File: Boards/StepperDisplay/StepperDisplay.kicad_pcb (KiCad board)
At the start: 2 copper layers, 120.4 x 102.1 mm, 113 parts, among them IC1 ATTINY861-P, P1 CONN_01X06, P2 ISP, Q1 BC857, Q10 BC857, Q11 BC857, Q12 BC857, Q13 BC857, Q14 BC857, Q15 BC857, Q16 BC857, Q17 BC857, Q18 BC857, Q2 BC857, Q3 BC857, Q4 BC857, Q5 BC857, Q6 BC857, Q7 BC857, Q8 BC857, Q9 BC857, SW1 SW_PUSH, SW2 SW_PUSH, U1 74HC595, U2 74HC595, U3 ULN2801A, U4 74HC595, U5 74HC595, U6 ULN2801A, U7 74HC595, U8 74HC595, U9 ULN2801A, X1 CRYSTAL_SMD

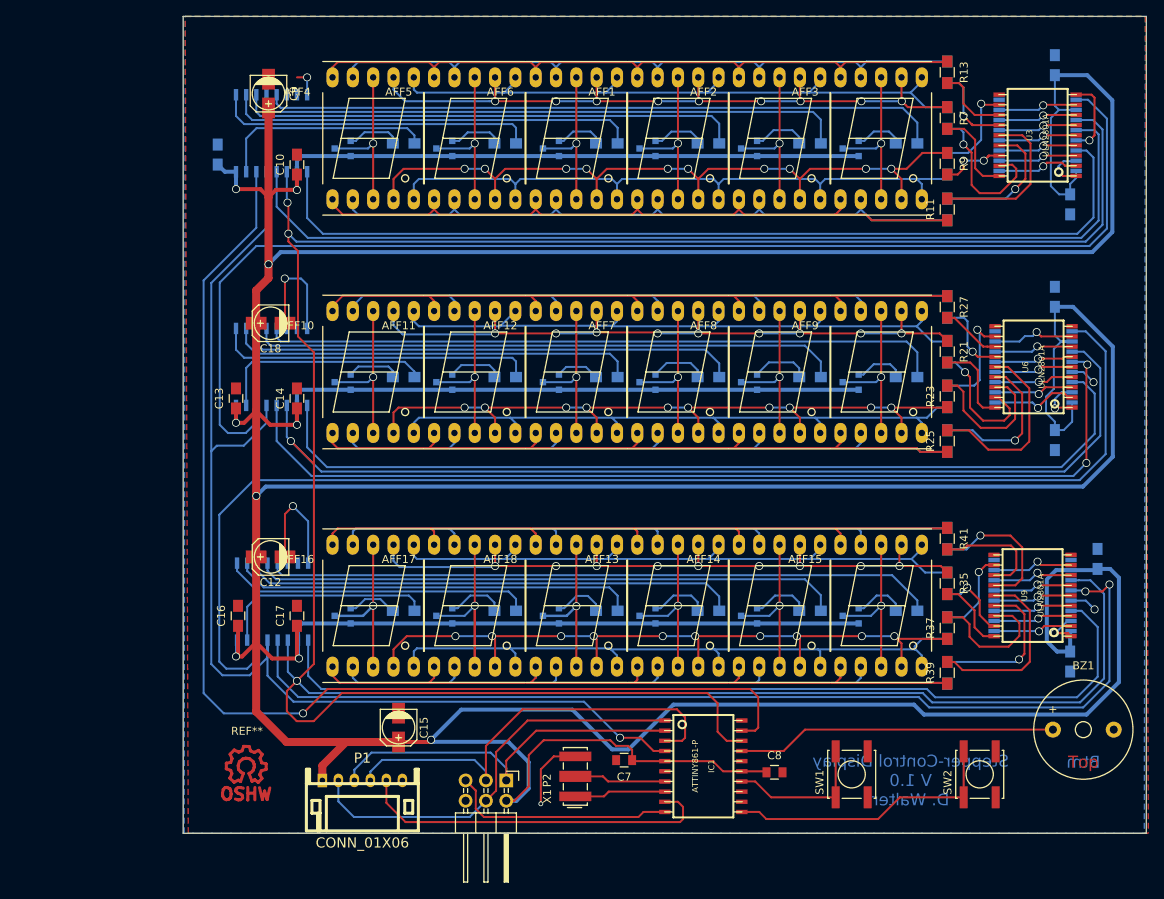
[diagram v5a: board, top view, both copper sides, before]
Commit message: Changed to segment multiplexing, new layout
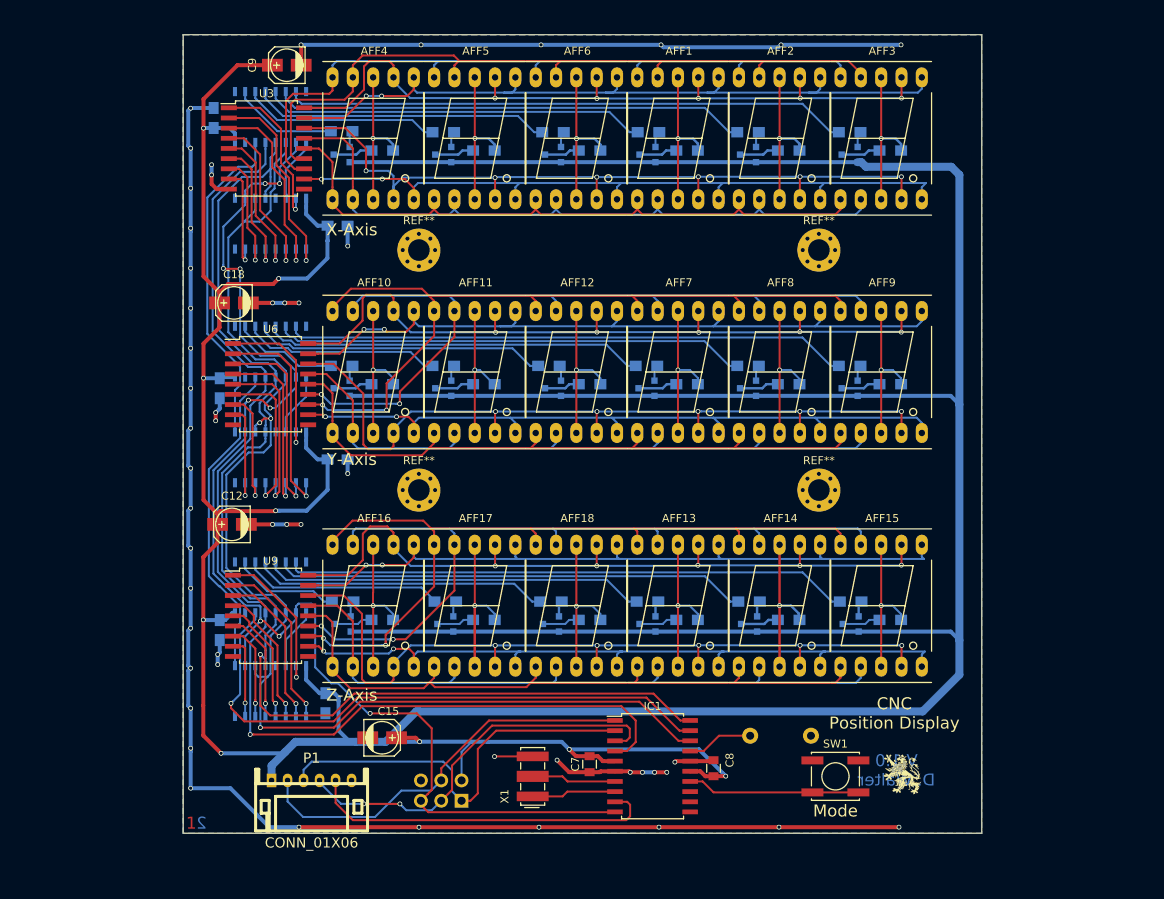
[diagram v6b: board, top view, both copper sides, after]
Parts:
- removed C1, C2, C3, C4, C5, C6: 100nF, Capacitors_SMD:C_0805_HandSoldering
- removed R13, R14, R27, R28, R41, R42: R, Resistors_SMD:R_0805_HandSoldering
- removed the REF** at (74.9, 133.1)
- removed SW2: SW_PUSH, Buttons_Switches_SMD:SW_SPST_EVPBF
- added G***: LOGO, Loewe:Loewe_Klein, F.Cu at (157.0, 134.1)
- added REF**: MountingHole_2.7mm_M2.5_Pad_Via, Mounting_Holes:MountingHole_2.7mm_M2.5_Pad_Via, F.Cu at (96.5, 98.6)
- added REF**: MountingHole_2.7mm_M2.5_Pad_Via, Mounting_Holes:MountingHole_2.7mm_M2.5_Pad_Via, F.Cu at (146.5, 98.6)
- added REF**: MountingHole_2.7mm_M2.5_Pad_Via, Mounting_Holes:MountingHole_2.7mm_M2.5_Pad_Via, F.Cu at (96.5, 68.6)
- added REF**: MountingHole_2.7mm_M2.5_Pad_Via, Mounting_Holes:MountingHole_2.7mm_M2.5_Pad_Via, F.Cu at (146.5, 68.6)
- BZ1, C10, C13, C14, C16, C17, R11, R21, R23, R25, R35, R37, R39, R7, R9: moved to B.Cu
- IC1: footprint w_smd_dil:soic-20 -> Housings_SOIC:SOIC-20_7.5x12.8mm_Pitch1.27mm
- P2: footprint Pin_Headers:Pin_Header_Angled_2x03 -> Pin_Headers:Pin_Header_Straight_2x03; moved to B.Cu
- Q1, Q10, Q11, Q12, Q13, Q14, Q15, Q16, Q17, Q18, Q2, Q3, Q4, Q5, Q6, Q7, Q8, Q9: footprint Housings_SOT-23_SOT-143_TSOT-6:SOT-23 -> TO_SOT_Packages_SMD:SOT-23
- U1, U2, U4, U5, U7, U8: footprint w_smd_dil:soic-16 -> SMD_Packages:SO-16-N
- U3, U6, U9: footprint w_smd_dil:soic-18 -> Housings_SOIC:SOIC-18_7.5x11.6mm_Pitch1.27mm
- moved U2 96.5 mm to (78.0, 65.3), turned to 180 degrees
- moved U3 96.4 mm to (77.5, 55.9), turned to 0 degrees
- moved U5 96.0 mm to (78.0, 94.5), turned to 180 degrees
- moved U8 96.0 mm to (78.0, 123.7), turned to 180 degrees
- moved U6 95.4 mm to (78.0, 85.3), turned to 0 degrees
- moved U9 95.3 mm to (78.0, 114.3), turned to 0 degrees
- moved R35 70.8 mm to (91.9, 114.8), turned to 0 degrees
- moved R21 70.7 mm to (91.9, 85.3), turned to 0 degrees
- moved R7 70.7 mm to (91.9, 56.1), turned to 0 degrees
- moved R36 58.1 mm to (104.6, 114.8), turned to 0 degrees
- moved R22 58.1 mm to (104.6, 85.3), turned to 0 degrees
- moved R8 58.1 mm to (104.6, 56.1), turned to 0 degrees
- moved R9 44.7 mm to (117.9, 56.1), turned to 0 degrees
- moved R23 44.7 mm to (117.9, 85.3), turned to 0 degrees
- moved R37 44.7 mm to (117.9, 114.8), turned to 0 degrees
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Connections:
- net CS renamed Net-(IC1-Pad9)
- net MISO renamed Net-(IC1-Pad2)
- net MOSI renamed Net-(IC1-Pad1)
- net SCK renamed Net-(IC1-Pad3)
- IC1 pad 10: Net-(IC1-Pad10) -> /Controller/Reset
- IC1 pad 11: Net-(IC1-Pad11) -> (no net)
- IC1 pad 19: /LEDsX/Ser_In -> /LEDsZ/Ser_In
- IC1 pad 20: (no net) -> /Controller/R_Clock
- P2 pad 5: Net-(IC1-Pad10) -> /Controller/Reset
- Q1 pad 3: Net-(AFF4-Pad3) -> Net-(Q1-Pad3)
- Q10 pad 3: Net-(AFF7-Pad3) -> Net-(Q10-Pad3)
- Q11 pad 3: Net-(AFF8-Pad3) -> Net-(Q11-Pad3)
- Q12 pad 3: Net-(AFF9-Pad3) -> Net-(Q12-Pad3)
- Q13 pad 3: Net-(AFF16-Pad3) -> Net-(Q13-Pad3)
- Q14 pad 3: Net-(AFF17-Pad3) -> Net-(Q14-Pad3)
- Q15 pad 3: Net-(AFF18-Pad3) -> Net-(Q15-Pad3)
- Q16 pad 3: Net-(AFF13-Pad3) -> Net-(Q16-Pad3)
- Q17 pad 3: Net-(AFF14-Pad3) -> Net-(Q17-Pad3)
- Q18 pad 3: Net-(AFF15-Pad3) -> Net-(Q18-Pad3)
- Q2 pad 3: Net-(AFF5-Pad3) -> Net-(Q2-Pad3)
- Q3 pad 3: Net-(AFF6-Pad3) -> Net-(Q3-Pad3)
- Q4 pad 3: Net-(AFF1-Pad3) -> Net-(Q4-Pad3)
- Q5 pad 3: Net-(AFF2-Pad3) -> Net-(Q5-Pad3)
- Q6 pad 3: Net-(AFF3-Pad3) -> Net-(Q6-Pad3)
- Q7 pad 3: Net-(AFF10-Pad3) -> Net-(Q7-Pad3)
- Q8 pad 3: Net-(AFF11-Pad3) -> Net-(Q8-Pad3)
- Q9 pad 3: Net-(AFF12-Pad3) -> Net-(Q9-Pad3)
- R10 pad 1: Net-(AFF1-Pad2) -> Net-(Q4-Pad3)
- R10 pad 2: Net-(R10-Pad2) -> Net-(AFF1-Pad3)
- R11 pad 1: Net-(AFF1-Pad1) -> Net-(Q5-Pad3)
- R11 pad 2: Net-(R11-Pad2) -> Net-(AFF2-Pad3)
- R12 pad 1: Net-(AFF1-Pad9) -> Net-(Q6-Pad3)
- R12 pad 2: Net-(R12-Pad2) -> Net-(AFF3-Pad3)
- R21 pad 1: Net-(AFF10-Pad7) -> Net-(Q7-Pad3)
- R21 pad 2: Net-(R21-Pad2) -> Net-(AFF10-Pad3)
- R22 pad 1: Net-(AFF10-Pad6) -> Net-(Q8-Pad3)
- R22 pad 2: Net-(R22-Pad2) -> Net-(AFF11-Pad3)
- R23 pad 1: Net-(AFF10-Pad4) -> Net-(Q9-Pad3)
- R23 pad 2: Net-(R23-Pad2) -> Net-(AFF12-Pad3)
- R24 pad 1: Net-(AFF10-Pad2) -> Net-(Q10-Pad3)
- R24 pad 2: Net-(R24-Pad2) -> Net-(AFF7-Pad3)
- R25 pad 1: Net-(AFF10-Pad1) -> Net-(Q11-Pad3)
- R25 pad 2: Net-(R25-Pad2) -> Net-(AFF8-Pad3)
- R26 pad 1: Net-(AFF10-Pad9) -> Net-(Q12-Pad3)
- R26 pad 2: Net-(R26-Pad2) -> Net-(AFF9-Pad3)
- R35 pad 1: Net-(AFF13-Pad7) -> Net-(Q13-Pad3)
- R35 pad 2: Net-(R35-Pad2) -> Net-(AFF16-Pad3)
- R36 pad 1: Net-(AFF13-Pad6) -> Net-(Q14-Pad3)
- R36 pad 2: Net-(R36-Pad2) -> Net-(AFF17-Pad3)
- R37 pad 1: Net-(AFF13-Pad4) -> Net-(Q15-Pad3)
- R37 pad 2: Net-(R37-Pad2) -> Net-(AFF18-Pad3)
- R38 pad 1: Net-(AFF13-Pad2) -> Net-(Q16-Pad3)
- R38 pad 2: Net-(R38-Pad2) -> Net-(AFF13-Pad3)
- R39 pad 1: Net-(AFF13-Pad1) -> Net-(Q17-Pad3)
- R39 pad 2: Net-(R39-Pad2) -> Net-(AFF14-Pad3)
- R40 pad 1: Net-(AFF13-Pad9) -> Net-(Q18-Pad3)
- R40 pad 2: Net-(R40-Pad2) -> Net-(AFF15-Pad3)
- R7 pad 1: Net-(AFF1-Pad7) -> Net-(Q1-Pad3)
- R7 pad 2: Net-(R7-Pad2) -> Net-(AFF4-Pad3)
- R8 pad 1: Net-(AFF1-Pad6) -> Net-(Q2-Pad3)
- R8 pad 2: Net-(R8-Pad2) -> Net-(AFF5-Pad3)
- R9 pad 1: Net-(AFF1-Pad4) -> Net-(Q3-Pad3)
- R9 pad 2: Net-(R9-Pad2) -> Net-(AFF6-Pad3)
- U1 pad 1: Net-(R2-Pad2) -> (no net)
- U1 pad 10: +5V -> /Controller/Reset
- U1 pad 12: /LEDsX/R_Clock -> /Controller/R_Clock
- U1 pad 15: Net-(R1-Pad2) -> (no net)
- U1 pad 2: Net-(R3-Pad2) -> Net-(R1-Pad2)
- U1 pad 3: Net-(R4-Pad2) -> Net-(R2-Pad2)
- U1 pad 4: Net-(R5-Pad2) -> Net-(R3-Pad2)
- U1 pad 5: Net-(R6-Pad2) -> Net-(R4-Pad2)
- U1 pad 6: (no net) -> Net-(R5-Pad2)
- U1 pad 7: (no net) -> Net-(R6-Pad2)
- U2 pad 10: +5V -> /Controller/Reset
- U2 pad 12: /LEDsX/R_Clock -> /Controller/R_Clock
- U2 pad 9: /LEDsY/Ser_In -> (no net)
- U3 pad 11: Net-(R14-Pad2) -> Net-(AFF1-Pad5)
- U3 pad 12: Net-(R13-Pad2) -> Net-(AFF1-Pad10)
- U3 pad 13: Net-(R12-Pad2) -> Net-(AFF1-Pad9)
- U3 pad 14: Net-(R11-Pad2) -> Net-(AFF1-Pad1)
- U3 pad 15: Net-(R10-Pad2) -> Net-(AFF1-Pad2)
- U3 pad 16: Net-(R9-Pad2) -> Net-(AFF1-Pad4)
- U3 pad 17: Net-(R8-Pad2) -> Net-(AFF1-Pad6)
- U3 pad 18: Net-(R7-Pad2) -> Net-(AFF1-Pad7)
- U4 pad 1: Net-(R16-Pad2) -> (no net)
- U4 pad 10: +5V -> /Controller/Reset
- U4 pad 12: /LEDsY/R_Clock -> /Controller/R_Clock
- U4 pad 15: Net-(R15-Pad2) -> (no net)
- U4 pad 2: Net-(R17-Pad2) -> Net-(R15-Pad2)
- U4 pad 3: Net-(R18-Pad2) -> Net-(R16-Pad2)
- U4 pad 4: Net-(R19-Pad2) -> Net-(R17-Pad2)
- U4 pad 5: Net-(R20-Pad2) -> Net-(R18-Pad2)
- U4 pad 6: (no net) -> Net-(R19-Pad2)
- U4 pad 7: (no net) -> Net-(R20-Pad2)
- U5 pad 10: +5V -> /Controller/Reset
- U5 pad 12: /LEDsY/R_Clock -> /Controller/R_Clock
- U5 pad 9: /LEDsZ/Ser_In -> /LEDsX/Ser_In
- U6 pad 11: Net-(R28-Pad2) -> Net-(AFF10-Pad5)
- U6 pad 12: Net-(R27-Pad2) -> Net-(AFF10-Pad10)
- U6 pad 13: Net-(R26-Pad2) -> Net-(AFF10-Pad9)
- U6 pad 14: Net-(R25-Pad2) -> Net-(AFF10-Pad1)
- U6 pad 15: Net-(R24-Pad2) -> Net-(AFF10-Pad2)
- U6 pad 16: Net-(R23-Pad2) -> Net-(AFF10-Pad4)
- U6 pad 17: Net-(R22-Pad2) -> Net-(AFF10-Pad6)
- U6 pad 18: Net-(R21-Pad2) -> Net-(AFF10-Pad7)
- U7 pad 1: Net-(R30-Pad2) -> (no net)
- U7 pad 10: +5V -> /Controller/Reset
- U7 pad 12: /LEDsZ/R_Clock -> /Controller/R_Clock
- U7 pad 15: Net-(R29-Pad2) -> (no net)
- U7 pad 2: Net-(R31-Pad2) -> Net-(R29-Pad2)
- U7 pad 3: Net-(R32-Pad2) -> Net-(R30-Pad2)
- U7 pad 4: Net-(R33-Pad2) -> Net-(R31-Pad2)
- U7 pad 5: Net-(R34-Pad2) -> Net-(R32-Pad2)
- U7 pad 6: (no net) -> Net-(R33-Pad2)
- U7 pad 7: (no net) -> Net-(R34-Pad2)
- U8 pad 10: +5V -> /Controller/Reset
- U8 pad 12: /LEDsZ/R_Clock -> /Controller/R_Clock
- U8 pad 9: (no net) -> /LEDsY/Ser_In
- U9 pad 11: Net-(R42-Pad2) -> Net-(AFF13-Pad5)
- U9 pad 12: Net-(R41-Pad2) -> Net-(AFF13-Pad10)
- U9 pad 13: Net-(R40-Pad2) -> Net-(AFF13-Pad9)
- U9 pad 14: Net-(R39-Pad2) -> Net-(AFF13-Pad1)
- U9 pad 15: Net-(R38-Pad2) -> Net-(AFF13-Pad2)
- U9 pad 16: Net-(R37-Pad2) -> Net-(AFF13-Pad4)
- U9 pad 17: Net-(R36-Pad2) -> Net-(AFF13-Pad6)
- U9 pad 18: Net-(R35-Pad2) -> Net-(AFF13-Pad7)
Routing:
- net /Controller/Ser_Clock: track 502.8 -> 159.6 mm, vias 4 -> 3
- net +5V: track 888.5 -> 629.5 mm
- net GND: track 57.9 -> 309.1 mm, vias 7 -> 51
- net /Controller/Reset: track 0.00 -> 159.8 mm, vias 0 -> 9
- net /Controller/R_Clock: track 0.00 -> 150.8 mm, vias 0 -> 1
- net /LEDsZ/R_Clock: track 128.8 -> 0.00 mm, vias 2 -> 0
- net /LEDsX/R_Clock: track 123.4 -> 0.00 mm
- net /LEDsY/R_Clock: track 122.6 -> 0.00 mm, vias 2 -> 0
- net /LEDsY/Ser_In: track 157.7 -> 40.4 mm
- net Net-(U7-Pad9): track 115.7 -> 7.66 mm
- net Net-(U1-Pad9): track 115.8 -> 8.04 mm
- net Net-(U4-Pad9): track 115.3 -> 7.91 mm
- net /LEDsX/Ser_In: track 146.0 -> 41.7 mm, vias 1 -> 0
- net /LEDsZ/Ser_In: track 158.3 -> 74.2 mm, vias 0 -> 1
- net Net-(IC1-Pad11): track 35.0 -> 0.00 mm
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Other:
- board size 120.4 x 102.1 mm -> 99.8 x 99.8 mm
- board text added: "1"
- board text added: "2"
- board text added: "CNC Position Display"
- board text added: "ISP"
- board text added: "Mode"
- board text added: "V 1.0 D. Walter"
- board text added: "X-Axis"
- board text added: "Y-Axis"
- board text added: "Z-Axis"
- board text removed: "Btm"
- board text removed: "Stepper-Control Display V 1.0 D. Walter"
- board text removed: "Top"

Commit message: Layout Release 1
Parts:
- P1: footprint w_conn_jst-ph:s6b-ph-kl -> w_conn_jst-ph:b6b-ph-kl; moved to B.Cu
- R1, R15, R16, R17, R18, R19, R2, R20, R29, R3, R30, R31, R32, R33, R34, R4, R5, R6: value R -> 1k
- R10, R11, R12, R21, R22, R23, R24, R25, R26, R35, R36, R37, R38, R39, R40, R7, R8, R9: value R -> 18R
- X1: value CRYSTAL_SMD -> 12MHz; footprint Crystals:Resonator_7.2x3mm -> Oscillator__Crystal_SMD:Resonator_CSTCE
- moved G*** 75.2 mm to (81.8, 135.1)
- moved C15 10.7 mm to (102.6, 128.5)
- moved P1 6.81 mm to (89.9, 134.6), turned to 180 degrees
- moved P2 6.36 mm to (108.2, 137.2)
- moved X1 2.79 mm to (113.3, 135.5)
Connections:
- REF** pad : (no net) -> GND (x4)
- X1 pad 2: Net-(IC1-Pad7) -> GND
- X1 pad 3: GND -> Net-(IC1-Pad7)
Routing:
- net +5V: track 629.5 -> 609.7 mm
- net Net-(IC1-Pad1): track 50.2 -> 34.9 mm, vias 0 -> 1
- net Net-(IC1-Pad2): track 51.0 -> 43.1 mm
- net Net-(IC1-Pad7): track 11.5 -> 6.86 mm
- net Net-(IC1-Pad8): track 11.4 -> 6.86 mm
- net Net-(IC1-Pad3): track 49.9 -> 46.8 mm, vias 2 -> 1
- net GND: track 309.1 -> 307.9 mm, vias 51 -> 52
- net /Controller/Reset: track 159.8 -> 158.7 mm
- net Net-(IC1-Pad9): track 44.3 -> 43.7 mm

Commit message: Layout updated
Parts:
- added Q19: BC817-40, TO_SOT_Packages_SMD:SOT-23, B.Cu at (151.1, 115.3)
- added R13: 1k, Resistors_SMD:R_0805_HandSoldering, F.Cu at (133.3, 128.9)
- Q1: value BC857 -> BC817-40; moved to F.Cu
- Q10, Q11, Q12, Q13, Q14, Q15, Q16, Q17, Q18, Q2, Q3, Q4, Q5, Q6, Q7, Q8, Q9: value BC857 -> BC817-40
- moved Q1 86.1 mm to (137.9, 126.0), turned to 0 degrees
- moved Q13 70.3 mm to (150.9, 85.9), turned to 0 degrees
- moved Q7 70.3 mm to (150.9, 56.9), turned to 0 degrees
- moved Q3 13.2 mm to (100.1, 56.9), turned to 0 degrees
- moved Q9 13.2 mm to (100.1, 85.9), turned to 0 degrees
- moved Q15 12.7 mm to (100.3, 115.3), turned to 0 degrees
- moved Q14 12.4 mm to (87.4, 115.3), turned to 0 degrees
- moved Q6 12.2 mm to (138.2, 56.9), turned to 0 degrees
- moved Q2 12.2 mm to (87.4, 56.9), turned to 0 degrees
- moved Q11 12.2 mm to (125.5, 85.9), turned to 0 degrees
- moved Q12 12.2 mm to (138.2, 85.9), turned to 0 degrees
- moved Q8 12.2 mm to (87.4, 85.9), turned to 0 degrees
- moved Q18 12.1 mm to (138.4, 115.3), turned to 0 degrees
- moved Q17 12.1 mm to (125.7, 115.3), turned to 0 degrees
- moved Q5 11.9 mm to (125.7, 56.9), turned to 0 degrees
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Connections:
- IC1 pad 17: Net-(BZ1-Pad1) -> Net-(IC1-Pad17)
- Q1 pad 2: +5V -> Net-(BZ1-Pad1)
- Q1 pad 3: Net-(Q1-Pad3) -> +5V
- Q10 pad 2: +5V -> Net-(Q10-Pad2)
- Q10 pad 3: Net-(Q10-Pad3) -> +5V
- Q11 pad 2: +5V -> Net-(Q11-Pad2)
- Q11 pad 3: Net-(Q11-Pad3) -> +5V
- Q12 pad 2: +5V -> Net-(Q12-Pad2)
- Q12 pad 3: Net-(Q12-Pad3) -> +5V
- Q13 pad 2: +5V -> Net-(Q13-Pad2)
- Q13 pad 3: Net-(Q13-Pad3) -> +5V
- Q14 pad 2: +5V -> Net-(Q14-Pad2)
- Q14 pad 3: Net-(Q14-Pad3) -> +5V
- Q15 pad 2: +5V -> Net-(Q15-Pad2)
- Q15 pad 3: Net-(Q15-Pad3) -> +5V
- Q16 pad 2: +5V -> Net-(Q16-Pad2)
- Q16 pad 3: Net-(Q16-Pad3) -> +5V
- Q17 pad 2: +5V -> Net-(Q17-Pad2)
- Q17 pad 3: Net-(Q17-Pad3) -> +5V
- Q18 pad 2: +5V -> Net-(Q18-Pad2)
- Q18 pad 3: Net-(Q18-Pad3) -> +5V
- Q2 pad 2: +5V -> Net-(Q2-Pad2)
- Q2 pad 3: Net-(Q2-Pad3) -> +5V
- Q3 pad 2: +5V -> Net-(Q3-Pad2)
- Q3 pad 3: Net-(Q3-Pad3) -> +5V
- Q4 pad 2: +5V -> Net-(Q4-Pad2)
- Q4 pad 3: Net-(Q4-Pad3) -> +5V
- Q5 pad 2: +5V -> Net-(Q5-Pad2)
- Q5 pad 3: Net-(Q5-Pad3) -> +5V
- Q6 pad 2: +5V -> Net-(Q6-Pad2)
- Q6 pad 3: Net-(Q6-Pad3) -> +5V
- Q7 pad 2: +5V -> Net-(Q7-Pad2)
- Q7 pad 3: Net-(Q7-Pad3) -> +5V
- Q8 pad 2: +5V -> Net-(Q8-Pad2)
- Q8 pad 3: Net-(Q8-Pad3) -> +5V
- Q9 pad 2: +5V -> Net-(Q9-Pad2)
- Q9 pad 3: Net-(Q9-Pad3) -> +5V
- R1 pad 1: Net-(Q1-Pad1) -> Net-(Q2-Pad1)
- R10 pad 1: Net-(Q4-Pad3) -> Net-(Q5-Pad2)
- R11 pad 1: Net-(Q5-Pad3) -> Net-(Q6-Pad2)
- R12 pad 1: Net-(Q6-Pad3) -> Net-(Q7-Pad2)
- R15 pad 1: Net-(Q7-Pad1) -> Net-(Q8-Pad1)
- R16 pad 1: Net-(Q8-Pad1) -> Net-(Q9-Pad1)
- R17 pad 1: Net-(Q9-Pad1) -> Net-(Q10-Pad1)
- R18 pad 1: Net-(Q10-Pad1) -> Net-(Q11-Pad1)
- R19 pad 1: Net-(Q11-Pad1) -> Net-(Q12-Pad1)
- R2 pad 1: Net-(Q2-Pad1) -> Net-(Q3-Pad1)
- R20 pad 1: Net-(Q12-Pad1) -> Net-(Q13-Pad1)
- R21 pad 1: Net-(Q7-Pad3) -> Net-(Q8-Pad2)
- R22 pad 1: Net-(Q8-Pad3) -> Net-(Q9-Pad2)
- R23 pad 1: Net-(Q9-Pad3) -> Net-(Q10-Pad2)
- R24 pad 1: Net-(Q10-Pad3) -> Net-(Q11-Pad2)
- R25 pad 1: Net-(Q11-Pad3) -> Net-(Q12-Pad2)
- R26 pad 1: Net-(Q12-Pad3) -> Net-(Q13-Pad2)
- R29 pad 1: Net-(Q13-Pad1) -> Net-(Q14-Pad1)
- R3 pad 1: Net-(Q3-Pad1) -> Net-(Q4-Pad1)
- R30 pad 1: Net-(Q14-Pad1) -> Net-(Q15-Pad1)
- R31 pad 1: Net-(Q15-Pad1) -> Net-(Q16-Pad1)
- R32 pad 1: Net-(Q16-Pad1) -> Net-(Q17-Pad1)
- R33 pad 1: Net-(Q17-Pad1) -> Net-(Q18-Pad1)
- R34 pad 1: Net-(Q18-Pad1) -> Net-(Q19-Pad1)
- R35 pad 1: Net-(Q13-Pad3) -> Net-(Q14-Pad2)
- R36 pad 1: Net-(Q14-Pad3) -> Net-(Q15-Pad2)
- R37 pad 1: Net-(Q15-Pad3) -> Net-(Q16-Pad2)
- R38 pad 1: Net-(Q16-Pad3) -> Net-(Q17-Pad2)
- R39 pad 1: Net-(Q17-Pad3) -> Net-(Q18-Pad2)
- R4 pad 1: Net-(Q4-Pad1) -> Net-(Q5-Pad1)
- R40 pad 1: Net-(Q18-Pad3) -> Net-(Q19-Pad2)
- R5 pad 1: Net-(Q5-Pad1) -> Net-(Q6-Pad1)
- R6 pad 1: Net-(Q6-Pad1) -> Net-(Q7-Pad1)
- R7 pad 1: Net-(Q1-Pad3) -> Net-(Q2-Pad2)
- R8 pad 1: Net-(Q2-Pad3) -> Net-(Q3-Pad2)
- R9 pad 1: Net-(Q3-Pad3) -> Net-(Q4-Pad2)
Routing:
- net +5V: track 609.7 -> 616.0 mm, vias 9 -> 10
- net Net-(BZ1-Pad1): track 8.29 -> 2.74 mm
- net Net-(Q12-Pad3): track 4.94 -> 0.00 mm
- net Net-(Q6-Pad3): track 4.94 -> 0.00 mm
- net Net-(Q8-Pad3): track 4.94 -> 0.00 mm
- net Net-(Q10-Pad3): track 4.94 -> 0.00 mm
- net Net-(Q2-Pad3): track 4.94 -> 0.00 mm
- net Net-(Q7-Pad3): track 4.94 -> 0.00 mm
- net Net-(Q5-Pad3): track 4.94 -> 0.00 mm
- net Net-(Q11-Pad3): track 4.94 -> 0.00 mm
- net Net-(Q1-Pad3): track 4.94 -> 0.00 mm
- net Net-(Q4-Pad3): track 4.81 -> 0.00 mm
- net Net-(Q18-Pad3): track 4.81 -> 0.00 mm
- net Net-(Q16-Pad3): track 4.81 -> 0.00 mm
- net Net-(Q13-Pad3): track 4.81 -> 0.00 mm
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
